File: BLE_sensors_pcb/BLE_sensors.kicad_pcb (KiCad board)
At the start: 2 copper layers, 9 parts, among them U1 BME280, U2 LSM303AHTR, U3 TPS63031DSK, U5 MCP73871, U6 TLV70018_SOT23-5

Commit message: Added schematic
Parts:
- C7, C8: value C_Small -> 4.7u
- C9: value C_Small -> 10u
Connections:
- U5 pad 17: unconnected-(U5-CE-Pad17) -> /PWR_SUPPLY/CE
- U5 pad 3: unconnected-(U5-SEL-Pad3) -> /PWR_SUPPLY/SEL
- U5 pad 4: unconnected-(U5-PROG2-Pad4) -> /PWR_SUPPLY/PROG2
- U5 pad 9: unconnected-(U5-~{TE}-Pad9) -> /PWR_SUPPLY/TE
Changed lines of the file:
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@@
 	(net 48 "Net-(U5-~{PG})")
 	(net 49 "Net-(U5-PROG1)")
-	(net 50 "unconnected-(U5-~{TE}-Pad9)")
-	(net 51 "unconnected-(U5-SEL-Pad3)")
-	(net 52 "Net-(U5-STAT2)")
-	(net 53 "unconnected-(U5-PROG2-Pad4)")
-	(net 54 "Net-(U5-PROG3)")
-	(net 55 "Net-(U5-STAT1{slash}~{LBO})")
-	(net 56 "unconnected-(U5-CE-Pad17)")
-	(net 57 "Net-(U5-THERM)")
-	(net 58 "unconnected-(U6-NC-Pad4)")
-	(net 59 "+1V8")
+	(net 50 "Net-(U5-STAT2)")
+	(net 51 "Net-(U5-PROG3)")
+	(net 52 "Net-(U5-STAT1{slash}~{LBO})")
+	(net 53 "Net-(U5-THERM)")
+	(net 54 "unconnected-(U6-NC-Pad4)")
+	(net 55 "+1V8")
+	(net 56 "/PWR_SUPPLY/CE")
+	(net 57 "/PWR_SUPPLY/SEL")
+	(net 58 "/PWR_SUPPLY/PROG2")
+	(net 59 "/PWR_SUPPLY/TE")
 	(footprint "Package_DFN_QFN:QFN-20-1EP_4x4mm_P0.5mm_EP2.5x2.5mm"
 		(layer "F.Cu")
@@
 			(layers "F.Cu" "F.Mask" "F.Paste")
 			(roundrect_rratio 0.25)
-			(net 51 "unconnected-(U5-SEL-Pad3)")
+			(net 57 "/PWR_SUPPLY/SEL")
 			(pinfunction "SEL")
 			(pintype "input")
@@
 			(layers "F.Cu" "F.Mask" "F.Paste")
 			(roundrect_rratio 0.25)
-			(net 53 "unconnected-(U5-PROG2-Pad4)")
+			(net 58 "/PWR_SUPPLY/PROG2")
 			(pinfunction "PROG2")
 			(pintype "input")
@@
 			(layers "F.Cu" "F.Mask" "F.Paste")
 			(roundrect_rratio 0.25)
-			(net 57 "Net-(U5-THERM)")
+			(net 53 "Net-(U5-THERM)")
 			(pinfunction "THERM")
 			(pintype "bidirectional")
@@
 			(layers "F.Cu" "F.Mask" "F.Paste")
 			(roundrect_rratio 0.25)
-			(net 52 "Net-(U5-STAT2)")
+			(net 50 "Net-(U5-STAT2)")
 			(pinfunction "STAT2")
 			(pintype "open_collector")
@@
 			(layers "F.Cu" "F.Mask" "F.Paste")
 			(roundrect_rratio 0.25)
-			(net 55 "Net-(U5-STAT1{slash}~{LBO})")
+			(net 52 "Net-(U5-STAT1{slash}~{LBO})")
 			(pinfunction "STAT1/~{LBO}")
 			(pintype "open_collector")
@@
 			(layers "F.Cu" "F.Mask" "F.Paste")
 			(roundrect_rratio 0.25)
-			(net 50 "unconnected-(U5-~{TE}-Pad9)")
+			(net 59 "/PWR_SUPPLY/TE")
 			(pinfunction "~{TE}")
 			(pintype "input")
@@
 			(layers "F.Cu" "F.Mask" "F.Paste")
 			(roundrect_rratio 0.25)
-			(net 54 "Net-(U5-PROG3)")
+			(net 51 "Net-(U5-PROG3)")
 			(pinfunction "PROG3")
 			(pintype "bidirectional")
@@
 			(layers "F.Cu" "F.Mask" "F.Paste")
 			(roundrect_rratio 0.25)
-			(net 56 "unconnected-(U5-CE-Pad17)")
+			(net 56 "/PWR_SUPPLY/CE")
 			(pinfunction "CE")
 			(pintype "input")
@@
 			)
 		)
-		(property "Value" "C_Small"
+		(property "Value" "4.7u"
 			(at 0 1.43 0)
 			(layer "F.Fab")
@@
 			)
 		)
-		(property "Value" "C_Small"
+		(property "Value" "4.7u"
 			(at 0 1.43 0)
 			(layer "F.Fab")
@@
 			(layers "F.Cu" "F.Mask" "F.Paste")
 			(roundrect_rratio 0.25)
-			(net 58 "unconnected-(U6-NC-Pad4)")
+			(net 54 "unconnected-(U6-NC-Pad4)")
 			(pinfunction "NC")
 			(pintype "no_connect")
@@
 			(layers "F.Cu" "F.Mask" "F.Paste")
 			(roundrect_rratio 0.25)
-			(net 59 "+1V8")
+			(net 55 "+1V8")
 			(pinfunction "OUT")
 			(pintype "power_out")
@@
 			)
 		)
-		(property "Value" "C_Small"
+		(property "Value" "10u"
 			(at 0 1.43 0)
 			(layer "F.Fab")

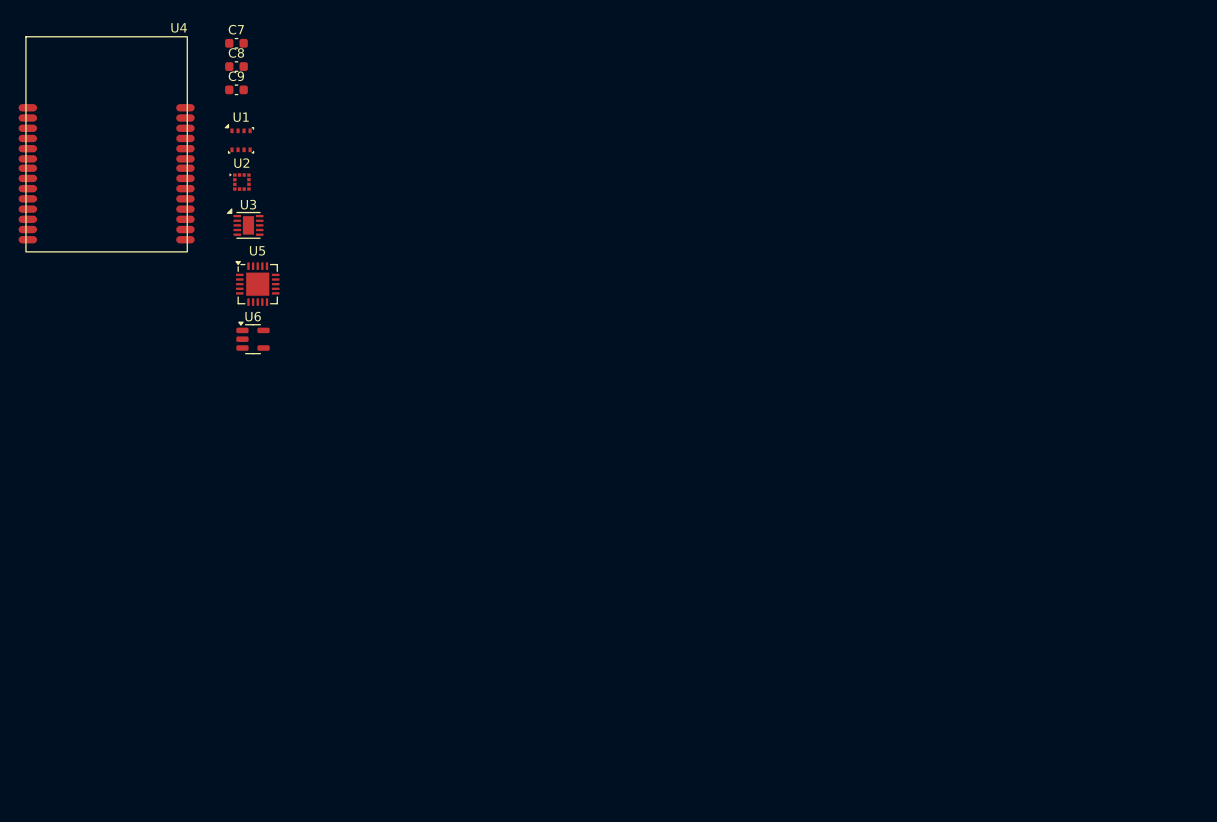
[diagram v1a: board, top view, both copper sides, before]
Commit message: Footprints and some pcb placement
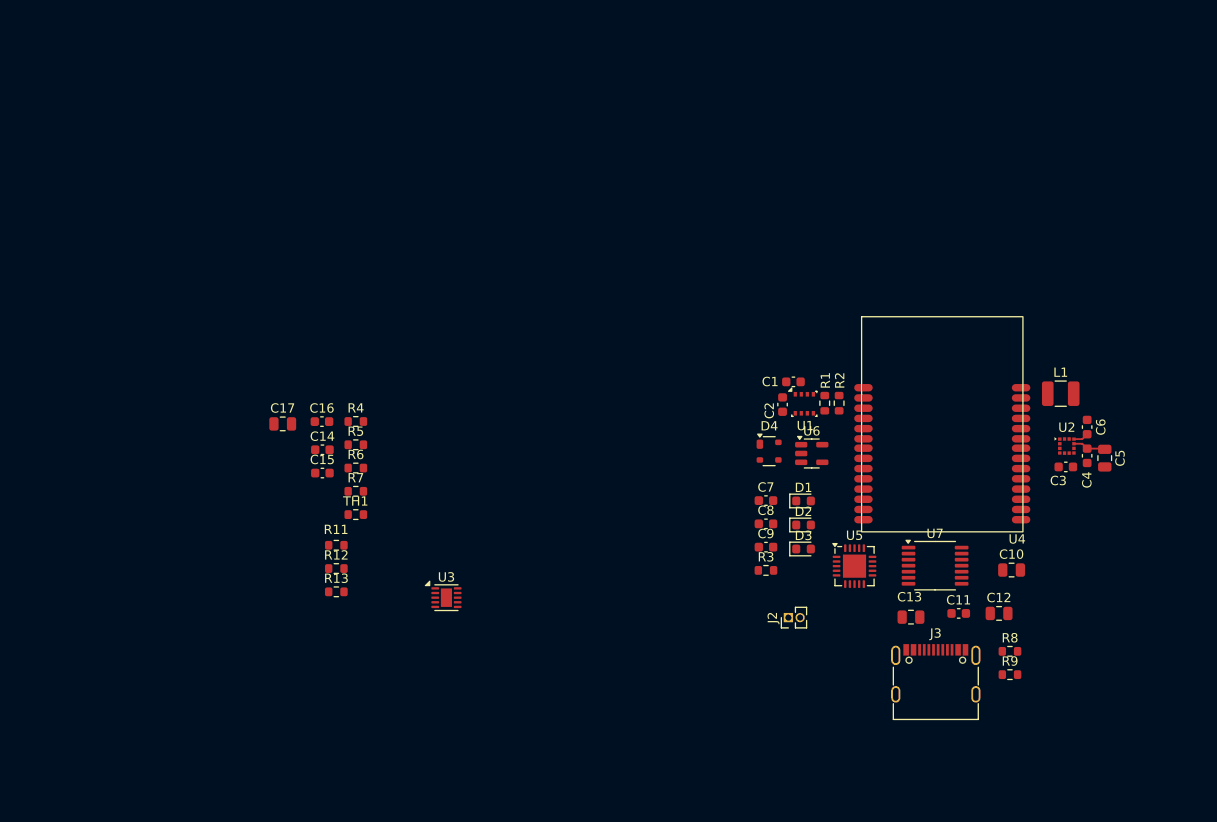
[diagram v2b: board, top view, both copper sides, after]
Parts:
- added C1: 0.1u, Capacitor_SMD:C_0603_1608Metric, F.Cu at (119.8, 63.7)
- added C10: 10u, Capacitor_SMD:C_0805_2012Metric, F.Cu at (143.3, 84.0)
- added C11: 0.1u, Capacitor_SMD:C_0603_1608Metric, F.Cu at (137.6, 88.7)
- added C12: 10u, Capacitor_SMD:C_0805_2012Metric, F.Cu at (141.9, 88.7)
- added C13: 10u, Capacitor_SMD:C_0805_2012Metric, F.Cu at (132.4, 89.0)
- added C14: 1u, Capacitor_SMD:C_0603_1608Metric, F.Cu at (69.0, 71.0)
- added C15: 1u, Capacitor_SMD:C_0603_1608Metric, F.Cu at (69.0, 73.5)
- added C16: 0.1u, Capacitor_SMD:C_0603_1608Metric, F.Cu at (68.9, 68.0)
- added C17: 4.7u, Capacitor_SMD:C_0805_2012Metric, F.Cu at (64.7, 68.2)
- added C2: 0.1u, Capacitor_SMD:C_0603_1608Metric, F.Cu at (118.6, 66.1)
- added C3: 0.1u, Capacitor_SMD:C_0603_1608Metric, F.Cu at (149.2, 72.8)
- added C4: 0.1u, Capacitor_SMD:C_0603_1608Metric, F.Cu at (151.4, 71.7)
- added C5: 10u, Capacitor_SMD:C_0805_2012Metric, F.Cu at (153.3, 71.9)
- added C6: 0.1u, Capacitor_SMD:C_0603_1608Metric, F.Cu at (151.4, 68.5)
- added D1: LED, LED_SMD:LED_0603_1608Metric, F.Cu at (120.9, 76.5)
- added D2: LED, LED_SMD:LED_0603_1608Metric, F.Cu at (120.9, 79.1)
- added D3: LED, LED_SMD:LED_0603_1608Metric, F.Cu at (120.9, 81.7)
- added D4: PRTR5V0U2X, Package_TO_SOT_SMD:SOT-143, F.Cu at (117.2, 71.2)
- added J2: Conn_01x02, Connector_PinHeader_1.27mm:PinHeader_1x02_P1.27mm_Vertical, F.Cu at (119.2, 89.1)
- added J3: USB_C_Receptacle, Connector_USB:USB_C_Receptacle_G-Switch_GT-USB-7010ASV, F.Cu at (135.1, 96.3)
- added L1: 1.5u, Inductor_SMD:L_1210_3225Metric, F.Cu at (148.6, 65.0)
- added R1: 4.7k, Resistor_SMD:R_0603_1608Metric, F.Cu at (123.2, 66.0)
- added R11: 5.11k, Resistor_SMD:R_0603_1608Metric, F.Cu at (70.5, 81.3)
- added R12: 5.11k, Resistor_SMD:R_0603_1608Metric, F.Cu at (70.5, 83.8)
- added R13: 1M, Resistor_SMD:R_0603_1608Metric, F.Cu at (70.5, 86.3)
- added R2: 4.7k, Resistor_SMD:R_0603_1608Metric, F.Cu at (124.7, 66.0)
- added R3: Rprog1, Resistor_SMD:R_0603_1608Metric, F.Cu at (116.8, 84.0)
- added R4: Rprog3, Resistor_SMD:R_0603_1608Metric, F.Cu at (72.6, 68.0)
- added R5: 470R, Resistor_SMD:R_0603_1608Metric, F.Cu at (72.6, 70.5)
- added R6: 470R, Resistor_SMD:R_0603_1608Metric, F.Cu at (72.6, 73.0)
- added R7: 470R, Resistor_SMD:R_0603_1608Metric, F.Cu at (72.6, 75.5)
- added R8: 22R, Resistor_SMD:R_0603_1608Metric, F.Cu at (143.1, 92.7)
- added R9: 22R, Resistor_SMD:R_0603_1608Metric, F.Cu at (143.1, 95.2)
- added TH1: 10k, Resistor_SMD:R_0603_1608Metric, F.Cu at (72.6, 78.0)
- added U7: MCP2221AxST, Package_SO:TSSOP-14_4.4x5mm_P0.65mm, F.Cu at (135.1, 83.5)
- U4: value ~ -> ME54BS01
- moved U4 95.0 mm to (135.8, 68.2)
- moved U2 93.4 mm to (149.3, 70.6)
- moved C7 75.5 mm to (116.8, 76.5)
- moved C8 75.5 mm to (116.8, 79.0)
- moved C9 75.5 mm to (116.8, 81.5)
- moved U5 71.2 mm to (126.4, 83.5)
- moved U1 67.1 mm to (121.0, 66.0)
- moved U6 61.5 mm to (121.8, 71.4)
- moved U3 45.5 mm to (82.3, 87.0)
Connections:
- U1 pad 2: /Temp Sensor/Vddio -> +1V8
- U1 pad 3: /Temp Sensor/SDA -> /SDA
- U1 pad 4: /Temp Sensor/SCL -> /SCL
- U1 pad 5: /Temp Sensor/SDO -> /SDO
- U1 pad 6: /Temp Sensor/Vddio -> +1V8
- U1 pad 8: /Temp Sensor/Vdd -> +1V8
- U2 pad 1: /Accelerometer-Magnetometer/SCL/SPC -> /SPC
- U2 pad 10: /Accelerometer-Magnetometer/Vdd_IO -> +3V3
- U2 pad 11: /Accelerometer-Magnetometer/INT2_XL -> /INT2_XL
- U2 pad 12: /Accelerometer-Magnetometer/INT1_XL -> /INT1_XL
- U2 pad 2: /Accelerometer-Magnetometer/CS -> /CS
- U2 pad 4: /Accelerometer-Magnetometer/SDI -> /SDI
- U2 pad 7: /Accelerometer-Magnetometer/INT_MAG/DRDY -> /INT_MAG/DRDY
- U2 pad 9: /Accelerometer-Magnetometer/Vdd -> +3V3
- U4 pad 19: /INT2_XL -> /SDI
- U4 pad 2: unconnected-(U4-P1.09-Pad2) -> /SCL
- U4 pad 21: /INT1_XL -> /CS
- U4 pad 22: /SDI -> /SPC
- U4 pad 23: /SPC -> /INT1_XL
- U4 pad 24: /CS -> /INT2_XL
- U4 pad 27: /SCL -> unconnected-(U4-P0.02-Pad27)
- U4 pad 28: /SDA -> unconnected-(U4-P0.03-Pad28)
- U4 pad 3: unconnected-(U4-P1.10-Pad3) -> /SDA
- U4 pad 4: unconnected-(U4-P1.11/AIN4-Pad4) -> /SDO
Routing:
- net +3V3: track 0.00 -> 5.22 mm
- net /SPC: track 0.00 -> 0.60 mm
- net /INT1_XL: track 0.00 -> 0.60 mm
- net /CS: track 0.00 -> 0.60 mm

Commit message: Initial pcb placement
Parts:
- added J1: Conn_ARM_SWD_TagConnect_TC2030-NL, Connector:Tag-Connect_TC2030-IDC-NL_2x03_P1.27mm_Vertical, F.Cu at (155.9, 71.0)
- added R10: 100k, Resistor_SMD:R_0603_1608Metric, F.Cu at (123.8, 75.9)
- added R14: 100k, Resistor_SMD:R_0603_1608Metric, F.Cu at (123.8, 79.1)
- added R15: 100R, Resistor_SMD:R_0603_1608Metric, F.Cu at (129.7, 73.8)
- added R16: 100R, Resistor_SMD:R_0603_1608Metric, F.Cu at (129.7, 75.4)
- moved R5 89.1 mm to (159.7, 89.0)
- moved R6 88.9 mm to (159.7, 90.6)
- moved R7 88.7 mm to (159.7, 92.2)
- moved R4 86.6 mm to (157.4, 85.6)
- moved TH1 86.0 mm to (157.2, 93.4), turned to -90 degrees
- moved R13 78.0 mm to (146.2, 105.3), turned to -90 degrees
- moved R11 74.9 mm to (143.3, 98.7), turned to -90 degrees
- moved C14 70.8 mm to (137.1, 90.5), turned to 90 degrees
- moved R12 69.5 mm to (138.4, 98.7), turned to -90 degrees
- moved C15 66.7 mm to (134.2, 87.1)
- moved C17 65.0 mm to (129.0, 78.1), turned to 180 degrees
- moved C16 61.4 mm to (129.2, 79.9), turned to 180 degrees
- moved U3 61.3 mm to (143.6, 89.9), turned to 90 degrees
- moved D3 42.4 mm to (158.3, 101.6), turned to 90 degrees
- moved D2 41.5 mm to (155.7, 101.6), turned to 90 degrees
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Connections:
- D4 pad 2: /usb-c/Protected_D- -> /usb-c/Protected_D+
- D4 pad 3: /usb-c/Protected_D+ -> /usb-c/Protected_D-
- U4 pad 12: unconnected-(U4-P1.04/AIN0-Pad12) -> Net-(U4-P1.04/AIN0)
- U4 pad 2: /SCL -> /SDA
- U4 pad 20: unconnected-(U4-NRESET-Pad20) -> /nRESET
- U4 pad 25: unconnected-(U4-SWDIO-Pad25) -> /SWDIO
- U4 pad 26: unconnected-(U4-SWDCLK-Pad26) -> /SWCLK
- U4 pad 27: unconnected-(U4-P0.02-Pad27) -> /SWO
- U4 pad 3: /SDA -> /SCL
- U4 pad 5: unconnected-(U4-P1.12/AIN5-Pad5) -> /TX
- U4 pad 6: unconnected-(U4-P1.13/AIN6-Pad6) -> /RX
- U5 pad 17: /PWR_SUPPLY/CE -> +5V
- U5 pad 3: /PWR_SUPPLY/SEL -> GND
- U5 pad 4: /PWR_SUPPLY/PROG2 -> +5V
- U5 pad 9: /PWR_SUPPLY/TE -> +5V
- U7 pad 5: /USB_to_Serial/URx -> Net-(U7-URx)
- U7 pad 6: /USB_to_Serial/UTx -> Net-(U7-UTx)
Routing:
- net /SWDIO: track 0.00 -> 8.33 mm
- net /INT_MAG/DRDY: track 0.00 -> 7.52 mm
- net /SWCLK: track 0.00 -> 7.18 mm
- net /INT2_XL: track 0.00 -> 6.69 mm
- net +3V3: track 5.22 -> 11.6 mm
- net /SWO: track 0.00 -> 5.35 mm
- net /INT1_XL: track 0.60 -> 5.68 mm
- net /PWR_SUPPLY/Buck-Boost/Vin: track 0.00 -> 4.62 mm
- net /SPC: track 0.60 -> 4.49 mm
- net Net-(U3-L1): track 0.00 -> 3.70 mm
- net /CS: track 0.60 -> 4.24 mm
- net Net-(U5-PROG1): track 0.00 -> 3.26 mm
- net /SDI: track 0.49 -> 3.75 mm
- net Net-(U3-L2): track 0.00 -> 2.78 mm
- net Net-(U5-~{PG}): track 0.00 -> 2.73 mm
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
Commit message: save
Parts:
- added R17: 10k, Resistor_SMD:R_0603_1608Metric, F.Cu at (154.8, 74.4)
- C10, C11, C12, C13, C16, C17, C7, C8, C9, D1, D2, D3, D4, J3, L1, R11, R12, R13, R3, R4, R5, R6, R7, R8, R9, TH1, U3, U5, U7: moved to B.Cu
- moved J2 20.5 mm to (147.6, 89.0)
- moved R13 19.1 mm to (133.5, 91.0), turned to 0 degrees
- moved C14 18.9 mm to (123.7, 77.1)
- moved R12 15.8 mm to (138.7, 82.9), turned to 0 degrees
- moved R9 15.7 mm to (133.6, 84.5), turned to 180 degrees
- moved J3 15.4 mm to (140.5, 89.9), turned to 180 degrees
- moved C15 15.3 mm to (126.7, 73.8)
- moved U6 15.3 mm to (126.8, 76.7)
- moved R8 15.0 mm to (133.6, 86.2), turned to 180 degrees
- moved R11 14.7 mm to (133.6, 87.7), turned to 0 degrees
- moved C12 14.5 mm to (141.3, 75.9), turned to 180 degrees
- moved L1 14.4 mm to (144.9, 79.4), turned to 90 degrees
- moved TH1 14.3 mm to (152.7, 79.8), turned to 0 degrees
- moved C13 12.2 mm to (141.3, 78.0), turned to 180 degrees
- moved R7 11.7 mm to (154.9, 81.5)
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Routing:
- net +1V8: track 0.00 -> 15.1 mm
- net Net-(J3-SHIELD): track 0.00 -> 14.6 mm
- net Net-(J3-D--PadA7): track 0.00 -> 10.4 mm
- net Net-(J3-D+-PadA6): track 0.00 -> 9.79 mm
- net /nRESET: track 0.00 -> 9.51 mm
- net /SDO: track 0.00 -> 7.92 mm
- net Net-(J3-CC2): track 0.00 -> 6.78 mm
- net /SDA: track 0.00 -> 6.15 mm
- net /SCL: track 0.00 -> 6.04 mm
- net /PWR_SUPPLY/Buck-Boost/Vin: track 4.62 -> 0.00 mm
- net Net-(J3-CC1): track 0.00 -> 4.30 mm
- net Net-(U3-L1): track 3.70 -> 0.00 mm
- net Net-(U4-P1.04/AIN0): track 0.00 -> 3.51 mm
- net Net-(U5-PROG1): track 3.26 -> 0.00 mm
- net Net-(U3-L2): track 2.78 -> 0.00 mm
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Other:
- board outline added: 37.8 x 24.9 mm
- copper layers 2 -> 4

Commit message: Added layers
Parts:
- moved R14 3.50 mm to (129.3, 82.2), turned to -90 degrees
- moved C17 2.54 mm to (123.3, 74.3), turned to 180 degrees
- moved C13 2.42 mm to (140.2, 75.8)
- moved C16 2.30 mm to (123.8, 76.6), turned to 180 degrees
- moved C12 2.24 mm to (140.2, 77.9)
- moved R7 2.00 mm to (155.8, 79.8)
- moved D4 1.97 mm to (128.9, 87.1)
- moved R5 1.81 mm to (155.8, 83.2)
- moved R6 1.79 mm to (155.8, 81.6)
- moved U7 1.71 mm to (126.7, 81.2)
- moved C11 1.66 mm to (137.8, 81.2), turned to 180 degrees
- moved L1 0.48 mm to (144.9, 79.8)
- moved R10 0.15 mm to (130.9, 82.2)
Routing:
- net GND: track 0.00 -> 40.3 mm, vias 0 -> 46
- net +3V3: track 10.6 -> 39.9 mm, vias 0 -> 9
- net +5V: track 2.60 -> 17.1 mm, vias 0 -> 9
- net /nRESET: track 9.51 -> 23.1 mm, vias 0 -> 2
- net /usb-c/Protected_D+: track 0.00 -> 11.7 mm
- net /PWR_SUPPLY/Buck-Boost/Vin: track 0.00 -> 10.3 mm
- net /usb-c/Protected_D-: track 0.00 -> 8.65 mm
- net +V_bat: track 0.00 -> 7.02 mm
- net Net-(U5-~{PG}): track 0.00 -> 3.57 mm
- net Net-(U3-L2): track 0.00 -> 3.08 mm
- net Net-(U5-STAT2): track 0.00 -> 2.83 mm
- net Net-(U3-L1): track 0.00 -> 2.53 mm
- net Net-(U5-STAT1/~{LBO}): track 0.00 -> 2.39 mm
- net Net-(U5-PROG3): track 0.00 -> 2.26 mm
- net Net-(U5-PROG1): track 0.00 -> 1.56 mm
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- added copper zone on In2.Cu, net +3V3
- added copper zone on In2.Cu, net +5V
- added copper zone on In1.Cu, net GND

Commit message: PCB rev1
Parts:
- moved R7 1.54 mm to (155.9, 81.3)
- moved R6 1.30 mm to (155.9, 82.9)
- moved R5 1.28 mm to (155.9, 84.4)
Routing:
- net +V_bat: track 7.02 -> 26.9 mm
- net GND: track 40.3 -> 51.5 mm, vias 46 -> 50
- net +5V: track 17.1 -> 27.5 mm
- net Net-(D3-K): track 0.00 -> 8.97 mm
- net Net-(D2-K): track 0.00 -> 7.91 mm
- net Net-(D1-K): track 0.00 -> 6.15 mm
- net Net-(U7-URx): track 0.00 -> 5.41 mm, vias 0 -> 1
- net Net-(J3-SHIELD): track 14.6 -> 18.8 mm
- net Net-(U7-UTx): track 0.00 -> 3.77 mm, vias 0 -> 1
- net Net-(U3-EN): track 1.00 -> 2.49 mm
- net +3V3: track 39.9 -> 40.8 mm
- net /usb-c/Protected_D+: track 11.7 -> 10.8 mm
- net Net-(U5-~{PG}): track 3.57 -> 2.97 mm
- net /PWR_SUPPLY/Buck-Boost/Vin: track 10.3 -> 9.77 mm
- net Net-(U5-STAT1/~{LBO}): track 2.39 -> 2.90 mm
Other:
- board size 37.8 x 24.9 mm -> 38.2 x 25.5 mm

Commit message: table
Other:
- board text added: "0"
- board text added: "0 mm"
- board text added: "0,01 mm"
- board text added: "0,02"
- board text added: "0,035 mm"
- board text added: "0,1 mm"
- board text added: "1"
- board text added: "1,24 mm"
- board text added: "3,3"
- board text added: "4,5"
- board text added: "B.Cu"
- board text added: "B.Mask"
- board text added: "B.Paste"
- board text added: "B.Silkscreen"
- board text added: "Bottom Silk Screen"
- board text added: "Bottom Solder Mask"
- board text added: "Bottom Solder Paste"
- board text added: "Color"
- board text added: "Dielectric"
- board text added: "Epsilon R"
- board text added: "F.Cu"
- board text added: "F.Mask"
- board text added: "F.Paste"
- board text added: "F.Silkscreen"
- board text added: "FR4"
- board text added: "In1.Cu"
- board text added: "In2.Cu"
- board text added: "Layer Name"
- board text added: "Loss Tangent"
- board text added: "Material"
- board text added: "Not specified"
- board text added: "Thickness (mm)"
- board text added: "Top Silk Screen"
- board text added: "Top Solder Mask"
- board text added: "Top Solder Paste"
- board text added: "Type"
- board text added: "copper"
- board text added: "core"
- board text added: "prepreg"
